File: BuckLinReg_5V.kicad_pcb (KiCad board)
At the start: 2 copper layers, 96 x 56 mm, 64 parts, among them J1 Barrel_Jack, J2 1x2 Male, J3 1x2 Male, J4 1x2 Male, Q1 PMBT2222, Q2 SQD40061EL, SW1 SW_SPDT, U1 TLV76050DBZT, U2 LMV358, U3 74HCT00, U4 SN74HCT02, U5 TCM810, U6 TPS56339DDC, U7 LM1084-5.0

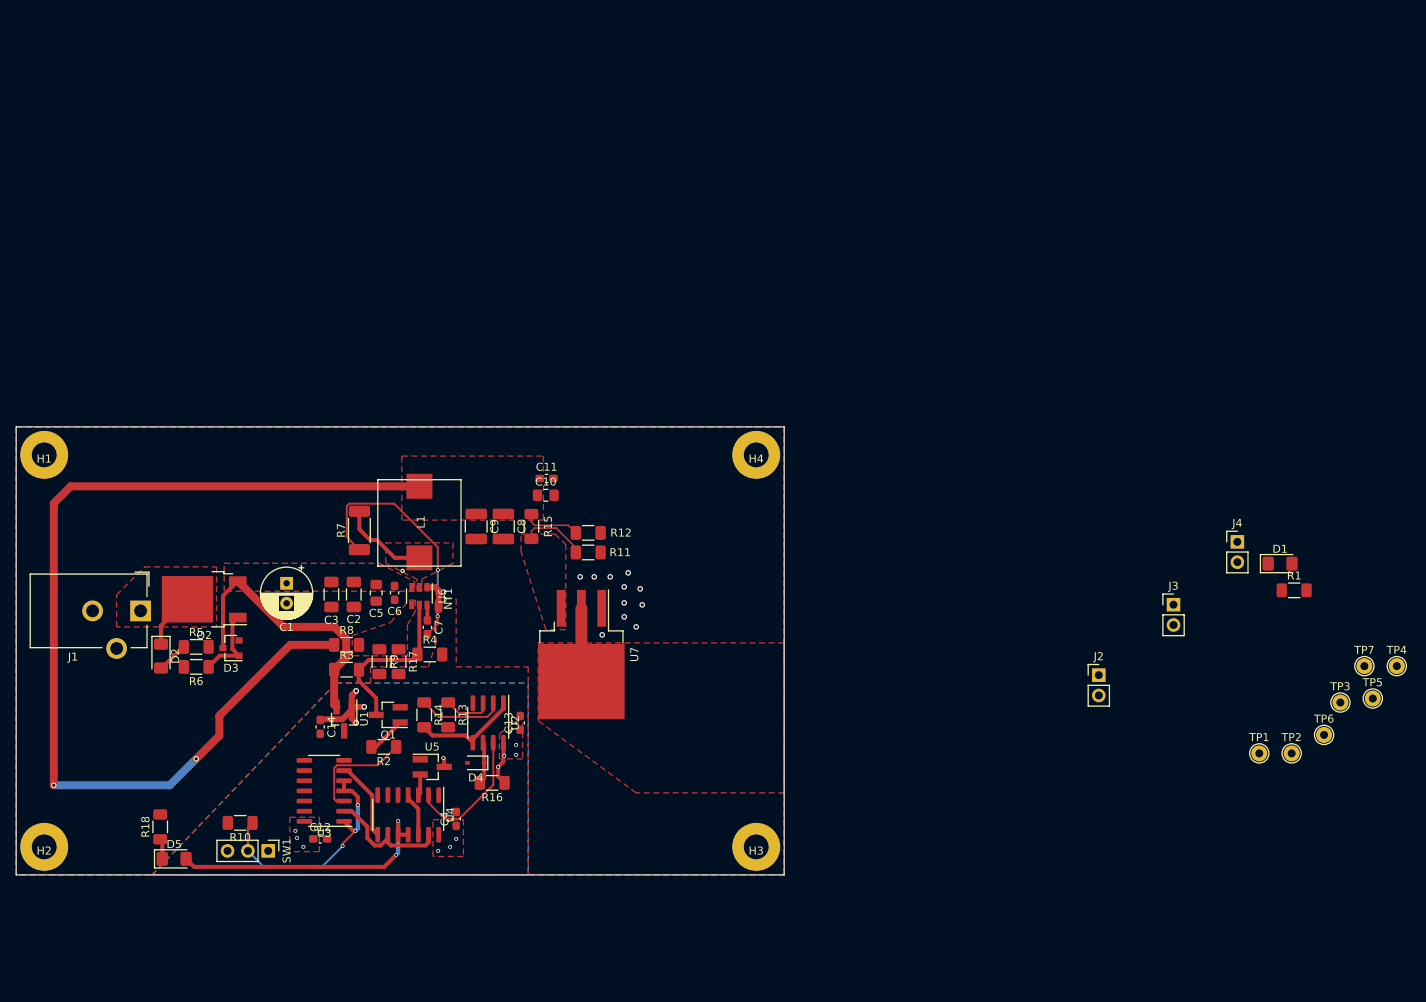
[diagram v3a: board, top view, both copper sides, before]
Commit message: Added testpoints and finished routing board
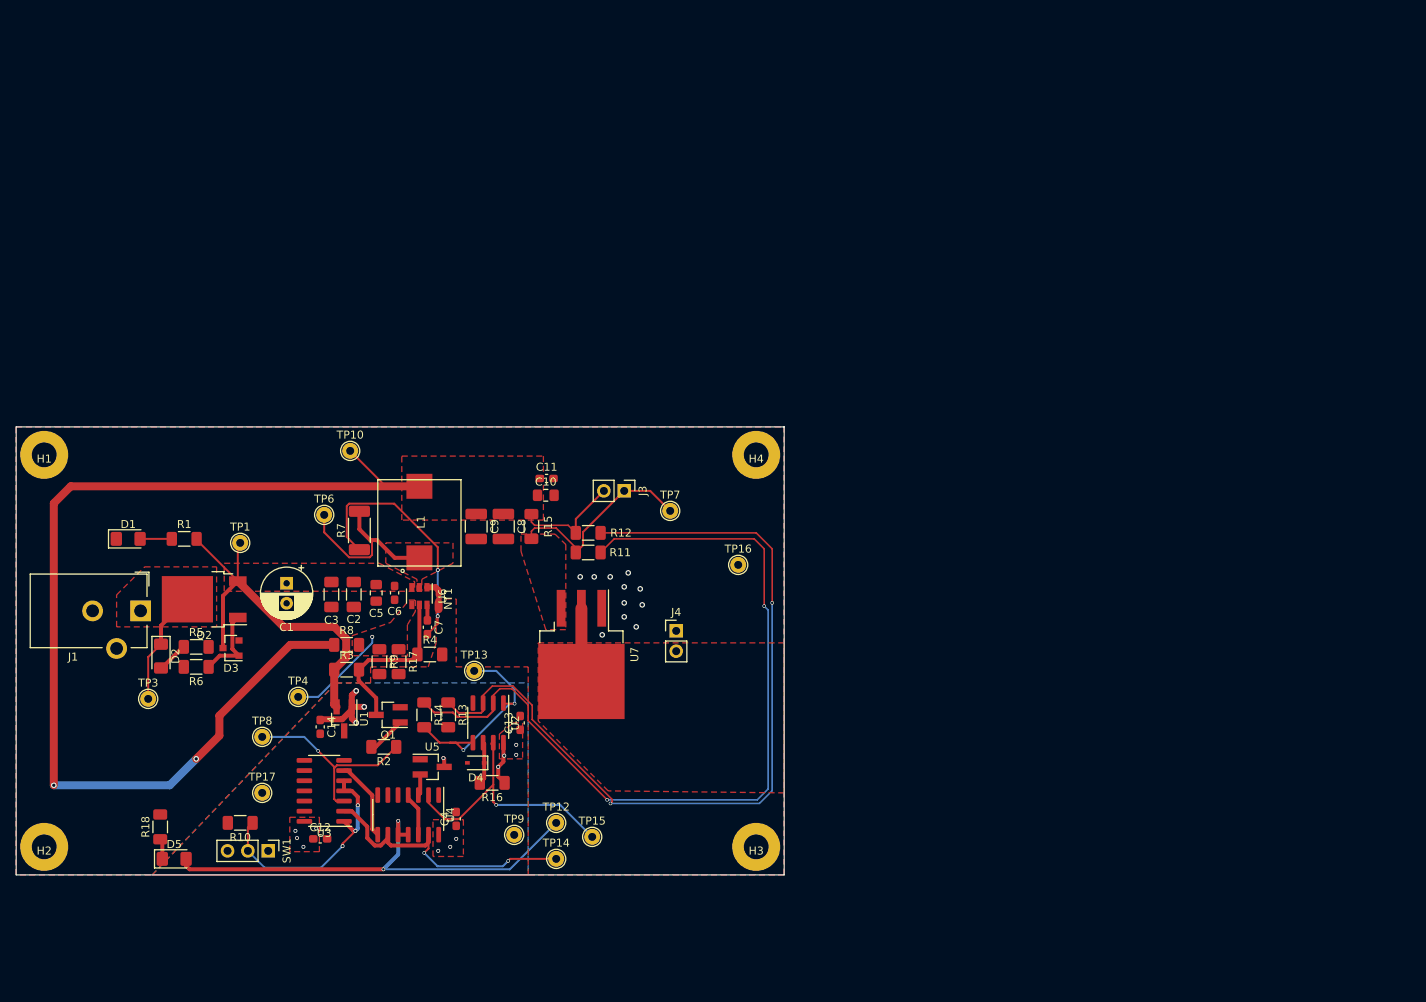
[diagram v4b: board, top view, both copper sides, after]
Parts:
- removed J2: 1x2 Male, Connector_PinHeader_2.54mm:PinHeader_1x02_P2.54mm_Vertical
- removed TP2: EN, TestPoint:TestPoint_THTPad_D2.0mm_Drill1.0mm
- removed TP5: BOOT, TestPoint:TestPoint_THTPad_D2.0mm_Drill1.0mm
- added TP10: SR+, TestPoint:TestPoint_THTPad_D2.0mm_Drill1.0mm, F.Cu at (99.8, 55.0)
- added TP12: Q, TestPoint:TestPoint_THTPad_D2.0mm_Drill1.0mm, F.Cu at (125.5, 101.5)
- added TP13: Iout, TestPoint:TestPoint_THTPad_D2.0mm_Drill1.0mm, F.Cu at (115.2, 82.5)
- added TP14: ~Q, TestPoint:TestPoint_THTPad_D2.0mm_Drill1.0mm, F.Cu at (125.5, 106.0)
- added TP15: OCPT, TestPoint:TestPoint_THTPad_D2.0mm_Drill1.0mm, F.Cu at (130.0, 103.2)
- added TP16: GNDP, TestPoint:TestPoint_THTPad_D2.0mm_Drill1.0mm, F.Cu at (148.2, 69.2)
- added TP17: GNDA, TestPoint:TestPoint_THTPad_D2.0mm_Drill1.0mm, F.Cu at (88.8, 97.8)
- added TP8: ~PWR_EN, TestPoint:TestPoint_THTPad_D2.0mm_Drill1.0mm, F.Cu at (88.8, 90.8)
- added TP9: 5V0, TestPoint:TestPoint_THTPad_D2.0mm_Drill1.0mm, F.Cu at (120.2, 103.0)
- moved TP3 149.0 mm to (74.5, 86.0)
- moved D1 144.0 mm to (72.0, 66.0)
- moved R1 138.9 mm to (79.0, 66.0)
- moved TP4 137.4 mm to (93.2, 85.8)
- moved TP1 130.1 mm to (86.0, 66.5)
- moved TP6 128.0 mm to (96.5, 63.0)
- moved TP7 88.9 mm to (139.8, 62.5)
- moved J4 71.0 mm to (140.5, 77.5)
- moved J3 70.1 mm to (134.0, 60.0), turned to 270 degrees
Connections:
- TP7 pad 1: /SR+ -> /SR-
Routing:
- net /DFA+: track 5.98 -> 104.4 mm, vias 0 -> 2
- net /DFA-: track 10.7 -> 105.7 mm, vias 0 -> 2
- net /Q: track 34.7 -> 59.5 mm
- net /~Q: track 16.3 -> 36.3 mm, vias 0 -> 2
- net /SR+: track 132.7 -> 149.9 mm
- net /SR-: track 8.28 -> 25.3 mm
- net /OCP_TRIGGER: track 17.1 -> 33.4 mm, vias 0 -> 1
- net /Vo: track 13.4 -> 27.0 mm, vias 0 -> 2
- net /FB: track 0.00 -> 12.8 mm, vias 0 -> 1
- net /+Vin: track 34.9 -> 47.2 mm
- net /SW: track 11.2 -> 22.8 mm
- net /~PWR_EN: track 14.1 -> 24.7 mm, vias 0 -> 1
- net /Vin: track 6.98 -> 14.5 mm
- net Net-(D1-Pad2): track 0.00 -> 3.96 mm

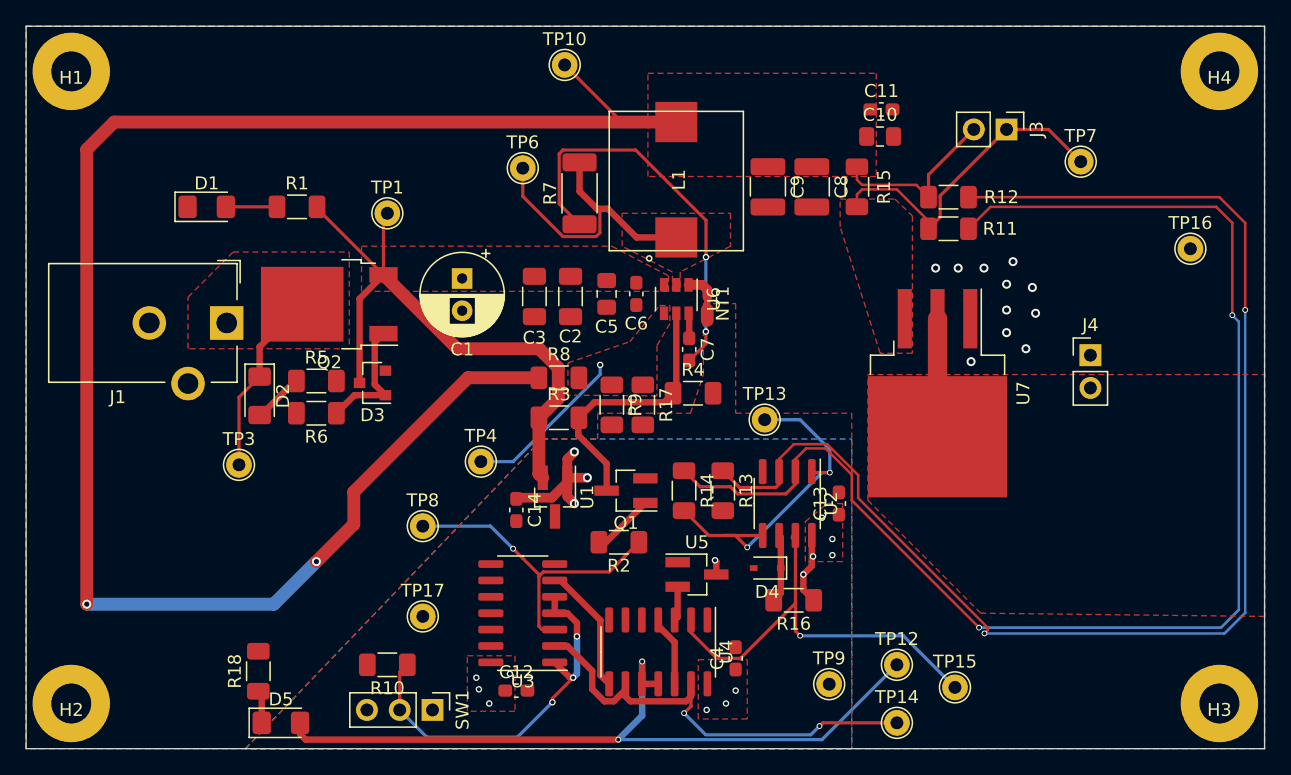
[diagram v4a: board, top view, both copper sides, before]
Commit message: Converted to 4-layer PCB.  Minimum track width 0.25 mm.
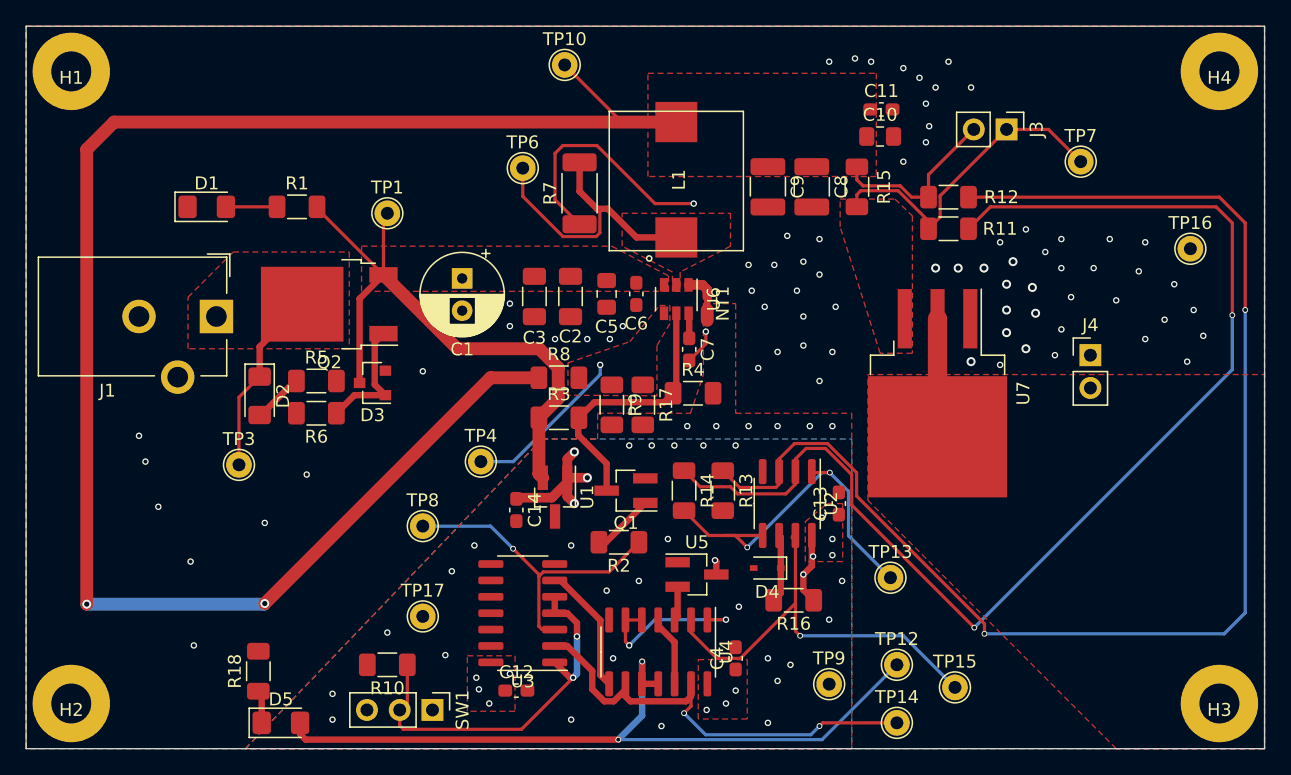
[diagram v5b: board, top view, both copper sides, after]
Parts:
- moved TP13 15.7 mm to (125.0, 94.8)
- moved J1 0.94 mm to (72.8, 74.5)
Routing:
- net Net-(U4-Pad1): track 0.00 -> 13.1 mm, vias 0 -> 2
- net /DFA-: track 105.7 -> 94.3 mm
- net /Vo: track 27.0 -> 29.3 mm
- net /SR+: track 149.9 -> 148.4 mm
- net Net-(C7-Pad2): track 31.3 -> 32.2 mm
- net /SW_SIG: track 29.7 -> 29.8 mm, vias 3 -> 2
- net GNDPWR: vias 11 -> 73
- net GNDA: vias 0 -> 31
- added copper zone on In2.Cu, net GNDA
- added copper zone on In1.Cu, net GNDPWR
- added copper zone on In2.Cu, net GNDPWR
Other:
- copper layers 2 -> 4
- net class Default: trace_width 0.2 -> 0.25
- rule trace_min: 0.2 -> 0.25

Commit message: Redid vias and fixed silkscreen overlap
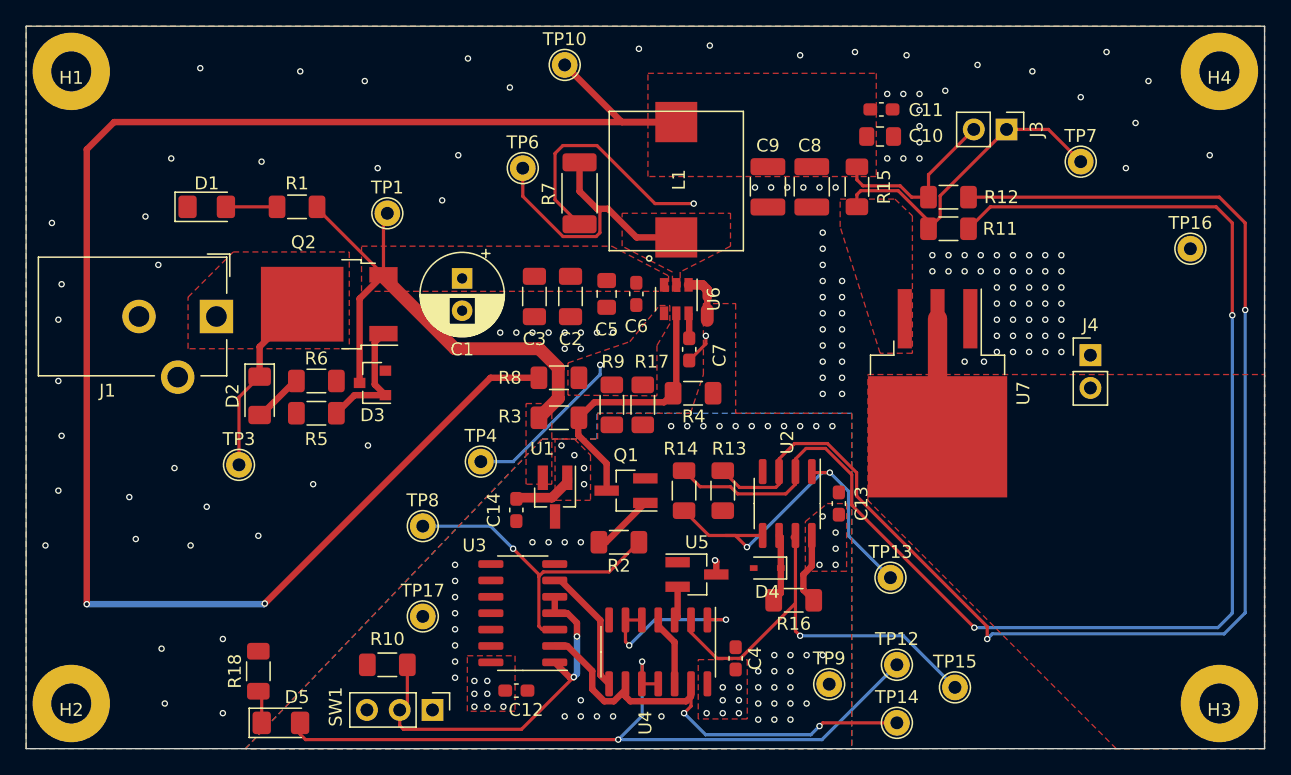
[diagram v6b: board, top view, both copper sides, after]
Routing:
- net /DFA-: track 94.3 -> 105.4 mm
- net /5V0_LOGIC: track 17.6 -> 11.6 mm, vias 16 -> 24
- net /+Vin: track 47.2 -> 42.6 mm
- net GNDPWR: vias 73 -> 134
- net GNDA: vias 31 -> 46

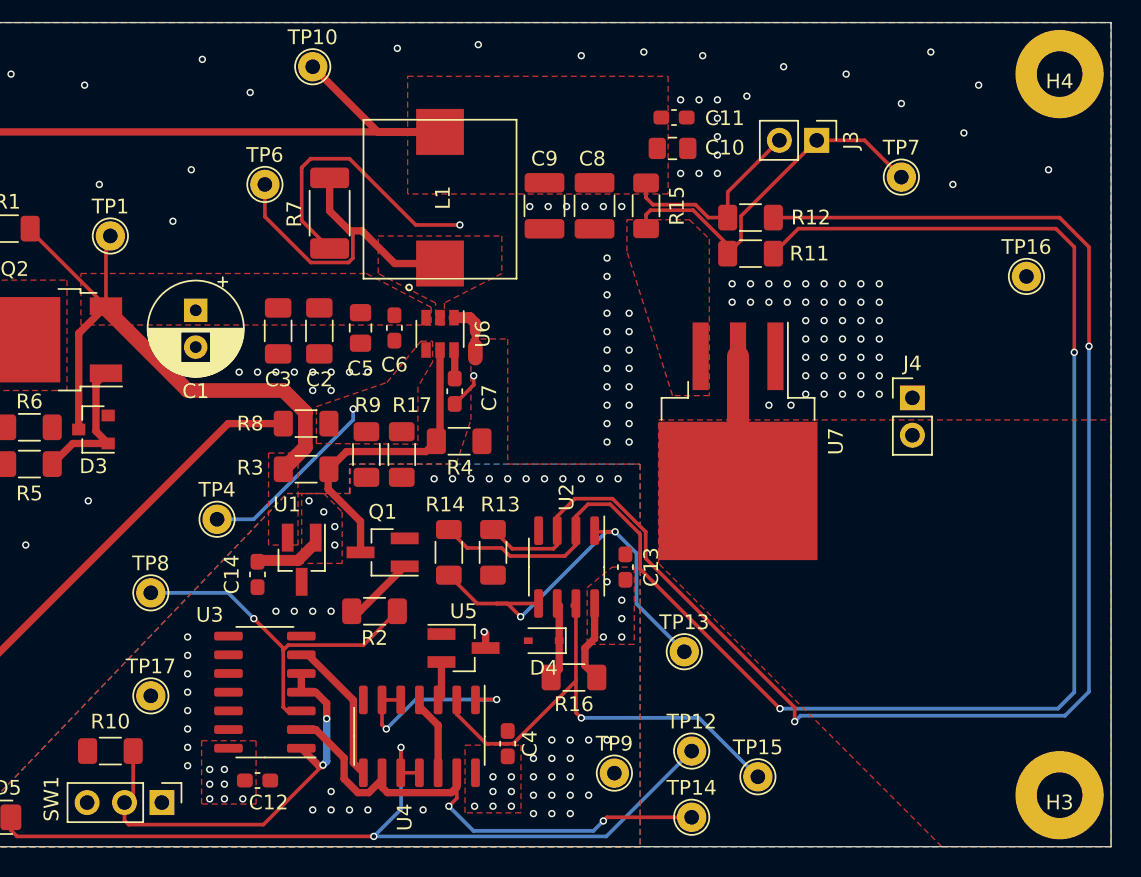
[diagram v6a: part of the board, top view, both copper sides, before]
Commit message: Added new power barrier connector.  Increased minimum copper to copper clearance to 0.21 mm.
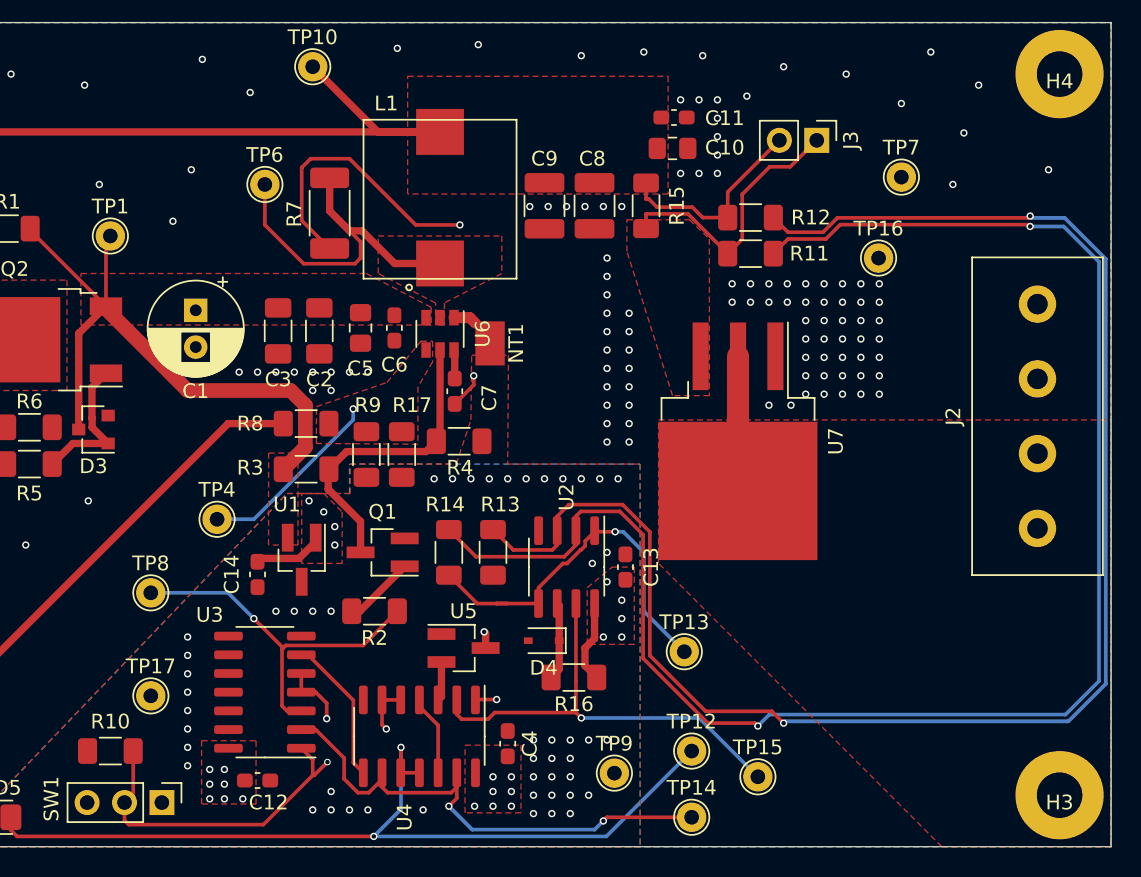
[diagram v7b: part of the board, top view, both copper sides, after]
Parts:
- removed J4: 1x2 Male, Connector_PinHeader_2.54mm:PinHeader_1x02_P2.54mm_Vertical
- added J2: 796638-4, BuckLinReg_5V:796636-4, F.Cu at (149.0, 78.8)
- NT1: footprint NetTie:NetTie-2_SMD_Pad0.5mm -> BuckLinReg_5V:NetShorter
- moved TP16 10.1 mm to (138.2, 68.0)
- moved NT1 1.04 mm to (111.8, 73.8)
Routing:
- net /DFA-: track 105.4 -> 112.1 mm
- net /SR-: track 25.2 -> 18.7 mm
- net /DFA+: track 104.8 -> 110.3 mm
- net /Vo: track 29.3 -> 26.2 mm, vias 2 -> 1
- net /OCP_TRIGGER: track 33.4 -> 31.0 mm
- net /SW: track 22.8 -> 23.9 mm
- net GNDA: track 0.80 -> 0.00 mm, vias 46 -> 49
- net GNDPWR: track 2.18 -> 1.61 mm
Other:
- net class Default: clearance 0.128 -> 0.21
- rule trace_clearance: 0.128 -> 0.21
